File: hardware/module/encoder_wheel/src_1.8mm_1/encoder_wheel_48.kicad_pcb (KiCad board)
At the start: 2 copper layers, 74 x 74 mm, 2 parts

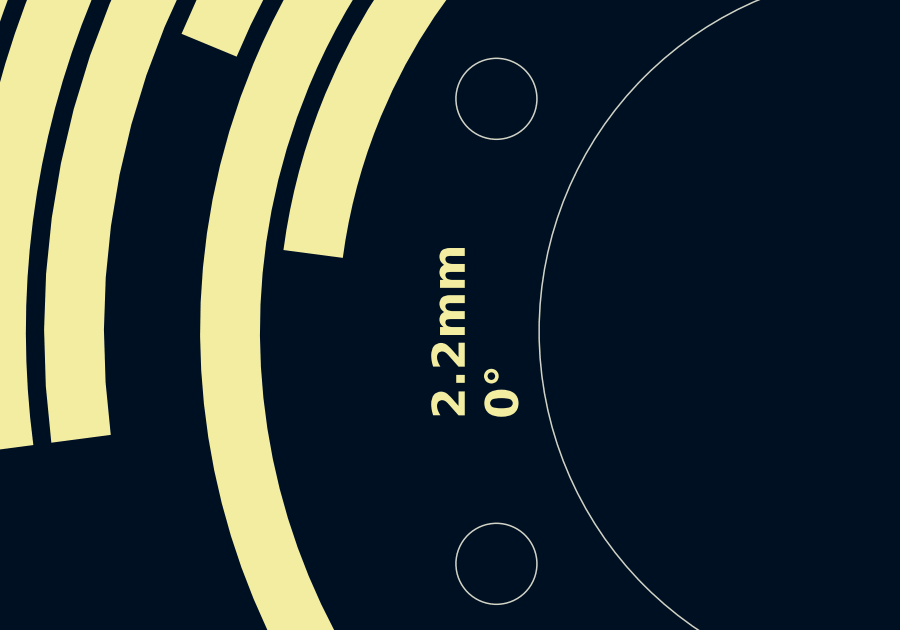
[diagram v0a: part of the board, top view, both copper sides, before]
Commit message: add encoder wheel variants
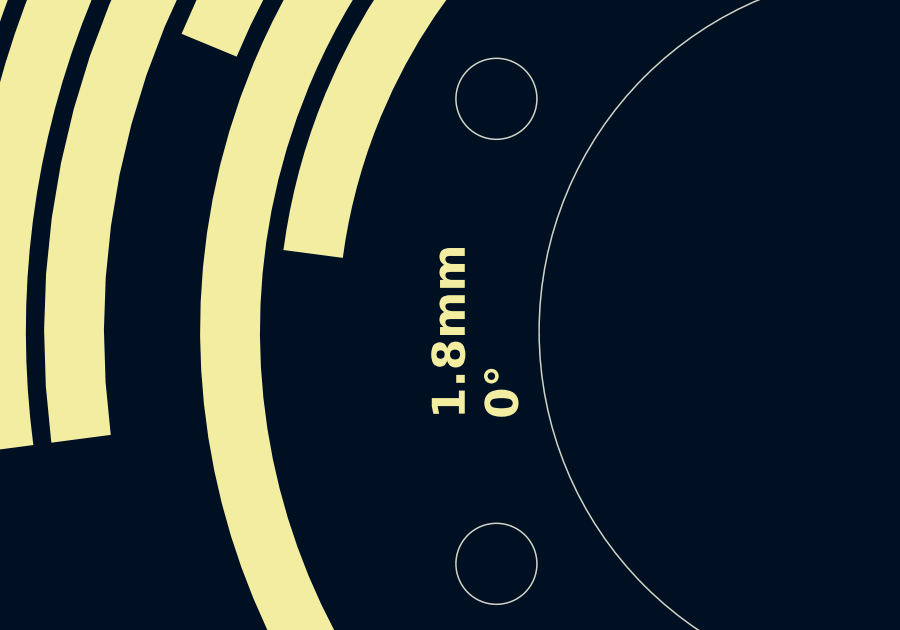
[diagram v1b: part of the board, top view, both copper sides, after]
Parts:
- REF** (x2): value OpenFlapEncoderPattern48_2.2mm -> OpenFlapEncoderPattern48_1.8mm; footprint EncoderPattern:OpenFlapEncoderPattern48_2.2mm -> EncoderPattern:OpenFlapEncoderPattern48_1.8mm
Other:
- board text added: "1.8mm 0°"
- board text added: "1.8mm 3.75°"
- board text removed: "2.2mm 0°"
- board text removed: "2.2mm 3.75°"
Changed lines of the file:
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@@
 	)
 	(net 0 "")
-	(footprint "EncoderPattern:OpenFlapEncoderPattern48_2.2mm"
+	(footprint "EncoderPattern:OpenFlapEncoderPattern48_1.8mm"
 		(layer "F.Cu")
 		(at 101 100)
@@
 			)
 		)
-		(property "Value" "OpenFlapEncoderPattern48_2.2mm"
+		(property "Value" "OpenFlapEncoderPattern48_1.8mm"
 			(at 0 1 0)
 			(unlocked yes)
@@
 			)
 		)
-		(property "Footprint" "EncoderPattern:OpenFlapEncoderPattern48_2.2mm"
+		(property "Footprint" "EncoderPattern:OpenFlapEncoderPattern48_1.8mm"
 			(at 0 0 0)
 			(unlocked yes)
@@
 		)
 	)
-	(footprint "EncoderPattern:OpenFlapEncoderPattern48_2.2mm"
+	(footprint "EncoderPattern:OpenFlapEncoderPattern48_1.8mm"
 		(layer "B.Cu")
 		(at 101 100 -176.25)
@@
 			)
 		)
-		(property "Value" "OpenFlapEncoderPattern48_2.2mm"
+		(property "Value" "OpenFlapEncoderPattern48_1.8mm"
 			(at 0 -1 3.75)
 			(unlocked yes)
@@
 			)
 		)
-		(property "Footprint" "EncoderPattern:OpenFlapEncoderPattern48_2.2mm"
+		(property "Footprint" "EncoderPattern:OpenFlapEncoderPattern48_1.8mm"
 			(at 0 0 3.75)
 			(unlocked yes)
@@
 		(layer "Edge.Cuts")
 	)
-	(gr_text "2.2mm \n3.75°"
+	(gr_text "1.8mm \n3.75°"
 		(at 88.427 97.333 90)
 		(layer "B.SilkS")
@@
 		)
 	)
-	(gr_text "2.2mm \n0°"
+	(gr_text "1.8mm \n0°"
 		(at 88.427 102.921 90)
 		(layer "F.SilkS")

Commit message: encoder changes
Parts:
- renumbered REF** to ENC1, REF** to ENC2

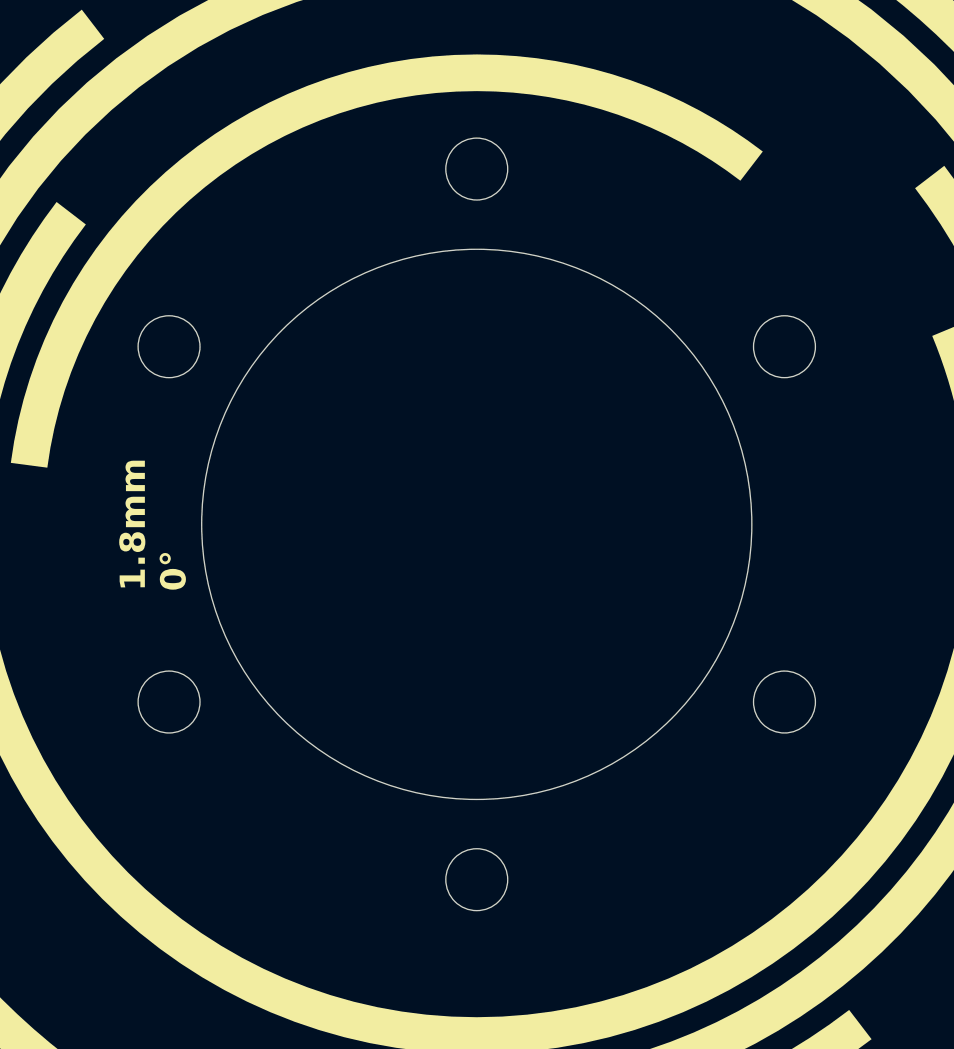
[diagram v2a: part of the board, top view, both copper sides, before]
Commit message: changed hole patern encoder wheel
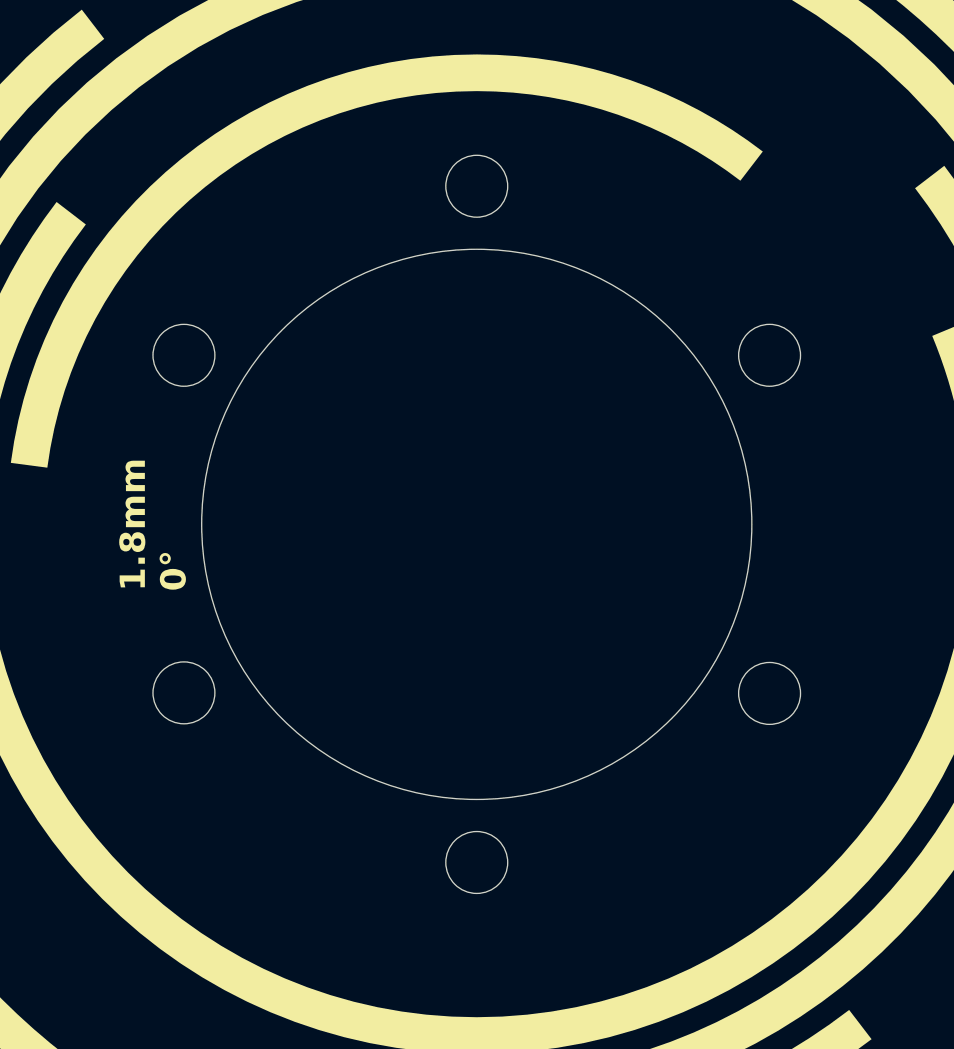
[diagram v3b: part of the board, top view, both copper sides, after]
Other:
- outline, holes or cut-outs redrawn
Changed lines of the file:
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@@
 				(xy -11.266715 -29.849949) (xy -10.281481 -30.203466) (xy -9.281621 -30.525345) (xy -8.267751 -30.81502)
 				(xy -8.682197 -32.362208) (xy -9.747476 -32.058296) (xy -10.797996 -31.720567) (xy -11.833111 -31.349614)
-				(xy -12.852178 -30.946031) (xy -13.854554 -30.510402) (xy -14.839593 -30.043327) (xy -15.806652 -29.545395)
+				(xy -12.852178 -30.946032) (xy -13.854554 -30.510402) (xy -14.839593 -30.043327) (xy -15.806652 -29.545395)
 				(xy -16.755088 -29.017199) (xy -15.952037 -27.627619)
 			)
@@
 				(xy 8.661965 -32.367899) (xy 7.619346 -32.628167) (xy 6.564163 -32.855757) (xy 5.496965 -33.050046)
 				(xy 4.4183 -33.21041) (xy 3.328719 -33.336223) (xy 2.228768 -33.426863) (xy 1.118999 -33.481705)
-				(xy -0.000041 -33.500124) (xy -0.001075 -33.500124) (xy -0.000556 -31.900225) (xy -0.000041 -31.900222)
+				(xy -0.000041 -33.500124) (xy -0.001075 -33.500124) (xy -0.000556 -31.900225) (xy -0.000041 -31.90022)
 				(xy 1.065218 -31.882664) (xy 2.121714 -31.830376) (xy 3.168918 -31.743958) (xy 4.2063 -31.624002)
 				(xy 5.23333 -31.471104) (xy 6.249476 -31.285859) (xy 7.254211 -31.06886) (xy 8.247002 -30.820704)
@@
 				(xy -23.637434 -21.416908) (xy -23.284883 -21.799537) (xy -22.926198 -22.176364) (xy -22.561452 -22.547308)
 				(xy -23.697817 -23.682639) (xy -24.457612 -22.897228) (xy -25.191642 -22.087376) (xy -25.899258 -21.253758)
-				(xy -26.579808 -20.39705) (xy -27.232652 -19.517927) (xy -27.857134 -18.617065) (xy -28.452607 -17.695141)
+				(xy -26.579806 -20.39705) (xy -27.232652 -19.517927) (xy -27.857134 -18.617065) (xy -28.452607 -17.695141)
 				(xy -29.018422 -16.752829) (xy -27.62781 -15.950812)
 			)
@@
 			(pts
 				(xy 18.806561 -24.521345) (xy 18.008705 -25.113995) (xy 17.19143 -25.681322) (xy 16.355315 -26.222746)
-				(xy 15.500938 -26.737683) (xy 14.628876 -27.225549) (xy 13.739707 -27.685761) (xy 12.834011 -28.117743)
+				(xy 15.500938 -26.737683) (xy 14.628876 -27.225549) (xy 13.739707 -27.685759) (xy 12.834011 -28.117743)
 				(xy 11.912364 -28.520903) (xy 10.975345 -28.894663) (xy 10.023531 -29.23844) (xy 9.057502 -29.551649)
 				(xy 8.077834 -29.83371) (xy 7.085106 -30.084038) (xy 6.079895 -30.302052) (xy 5.062781 -30.487168)
@@
 				(xy -17.828925 23.247311) (xy -18.806127 24.521135) (xy -18.008283 25.11377) (xy -17.191027 25.681088)
 				(xy -16.354937 26.222504) (xy -15.500589 26.737436) (xy -14.628561 27.225301) (xy -13.73943 27.685516)
-				(xy -12.833772 28.117497) (xy -11.912166 28.520661) (xy -10.975189 28.894428) (xy -10.023417 29.238206)
-				(xy -9.057427 29.551421) (xy -8.077795 29.833486) (xy -7.085104 30.083819) (xy -6.079929 30.301836)
+				(xy -12.833772 28.117497) (xy -11.912166 28.520661) (xy -10.975189 28.894429) (xy -10.023417 29.238206)
+				(xy -9.057427 29.551421) (xy -8.077795 29.833486) (xy -7.085104 30.083819) (xy -6.07993 30.301836)
 				(xy -5.062838 30.486955) (xy -4.034419 30.638591)
 			)
@@
 				(xy -17.090735 -23.796679) (xy -16.304792 -24.343111) (xy -15.500463 -24.864257) (xy -14.678322 -25.359541)
 				(xy -13.838943 -25.828387) (xy -12.982901 -26.270221) (xy -12.110771 -26.684465) (xy -11.223127 -27.070544)
-				(xy -11.837043 -28.552111) (xy -12.773694 -28.145174) (xy -13.693928 -27.70851) (xy -14.597134 -27.242726)
+				(xy -11.837043 -28.552111) (xy -12.773694 -28.145174) (xy -13.69393 -27.70851) (xy -14.597134 -27.242726)
 				(xy -15.482717 -26.748428) (xy -16.350072 -26.226223) (xy -17.198594 -25.676718) (xy -18.02768 -25.10052)
-				(xy -18.836728 -24.498237) (xy -19.625135 -23.870473) (xy -20.392296 -23.217837) (xy -21.137612 -22.540936)
+				(xy -18.836728 -24.498237) (xy -19.625135 -23.870473) (xy -20.392296 -23.217837) (xy -21.137613 -22.540936)
 				(xy -21.860471 -21.840376) (xy -22.560278 -21.116764) (xy -23.236427 -20.370707) (xy -23.888314 -19.602811)
 				(xy -24.515338 -18.813685) (xy -23.24203 -17.835966)
@@
 				(xy 22.135658 14.92714) (xy 21.120306 16.329401) (xy 20.018367 17.661261) (xy 18.833957 18.918605)
 				(xy 17.571194 20.097317) (xy 16.234196 21.193282) (xy 14.827081 22.202386) (xy 13.353966 23.120514)
-				(xy 11.818969 23.94355) (xy 10.226209 24.66738) (xy 10.84116 26.149976)
+				(xy 11.818969 23.94355) (xy 10.226209 24.66738) (xy 10.841161 26.149976)
 			)
 			(stroke
@@
 				(xy -28.296811 -0.467562) (xy -28.300636 0.000154) (xy -28.250268 1.703391) (xy -28.101061 3.379906)
 				(xy -27.855866 5.026858) (xy -27.517533 6.641405) (xy -27.088911 8.220705) (xy -26.572849 9.761917)
-				(xy -25.972198 11.2622) (xy -25.289807 12.718712) (xy -24.528525 14.128612) (xy -23.691206 15.489057)
+				(xy -25.972198 11.2622) (xy -25.289807 12.718712) (xy -24.528525 14.128612) (xy -23.691208 15.489057)
 				(xy -22.78069 16.797208) (xy -21.799835 18.050221) (xy -20.751489 19.245257) (xy -19.6385 20.379472)
 				(xy -18.463719 21.450027) (xy -17.229995 22.454078)
@@
 				(xy -29.237832 -1.924824) (xy -29.202875 -2.401023) (xy -29.160371 -2.875098) (xy -29.110401 -3.346999)
 				(xy -29.053045 -3.816668) (xy -30.639512 -4.025443) (xy -30.699902 -3.530123) (xy -30.752548 -3.03244)
-				(xy -30.797354 -2.532453) (xy -30.834229 -2.030208) (xy -30.863069 -1.525771) (xy -30.883788 -1.019194)
+				(xy -30.797354 -2.532454) (xy -30.83423 -2.030208) (xy -30.863069 -1.525771) (xy -30.883788 -1.019194)
 				(xy -30.896289 -0.510533) (xy -30.900478 0.000154) (xy -30.890729 0.78352) (xy -30.861641 1.56206)
 				(xy -30.813448 2.335546) (xy -30.746385 3.103753) (xy -30.660688 3.866454) (xy -30.556591 4.62342)
@@
 				(xy -10.83142 -26.153803) (xy -10.216987 -24.67121) (xy -9.623267 -24.909187) (xy -9.022652 -25.133286)
 				(xy -8.415338 -25.343305) (xy -7.801522 -25.539039) (xy -7.1814 -25.720284) (xy -6.555168 -25.886838)
-				(xy -5.923023 -26.038495) (xy -5.285163 -26.175054) (xy -4.641777 -26.296309) (xy -3.993074 -26.402058)
+				(xy -5.923023 -26.038495) (xy -5.285163 -26.175054) (xy -4.641775 -26.296309) (xy -3.993074 -26.402058)
 				(xy -3.339241 -26.492097) (xy -2.680477 -26.566221) (xy -2.016979 -26.624228) (xy -1.348942 -26.665914)
 				(xy -0.676564 -26.691075) (xy -0.000041 -26.699507) (xy 1.140178 -26.675552) (xy 2.268208 -26.604328)
@@
 				(xy 11.013382 -20.312902) (xy 10.017318 -20.822849) (xy 8.993996 -21.285266) (xy 7.944866 -21.698708)
 				(xy 6.871376 -22.061717) (xy 5.774973 -22.372854) (xy 4.657106 -22.630667) (xy 3.519223 -22.83371)
-				(xy 2.362772 -22.980533) (xy 1.189201 -23.069689) (xy -0.000041 -23.09973) (xy -1.189285 -23.069689)
+				(xy 2.362772 -22.980533) (xy 1.189201 -23.069689) (xy -0.000041 -23.09973) (xy -1.189286 -23.069689)
 				(xy -2.362848 -22.980533) (xy -3.519292 -22.83371) (xy -4.657166 -22.630667) (xy -5.775021 -22.372854)
 				(xy -6.871409 -22.061717) (xy -7.944884 -21.698705) (xy -8.993996 -21.285266) (xy -10.017299 -20.822849)
@@
 	)
 	(gr_circle
-		(center 87.576606 107.75)
-		(end 88.926606 107.75)
+		(center 88.226125 107.35)
+		(end 89.576125 107.35)
 		(stroke
 			(width 0.05)
@@
 	)
 	(gr_circle
-		(center 101 84.5)
-		(end 102.35 84.5)
-		(stroke
-			(width 0.05)
-			(type default)
-		)
-		(fill none)
-		(layer "Edge.Cuts")
-	)
-	(gr_circle
-		(center 114.423394 92.25)
-		(end 115.773394 92.25)
-		(stroke
-			(width 0.05)
-			(type default)
-		)
-		(fill none)
-		(layer "Edge.Cuts")
-	)
-	(gr_circle
-		(center 87.576606 92.25)
-		(end 88.926606 92.25)
+		(center 101 85.25)
+		(end 102.35 85.25)
+		(stroke
+			(width 0.05)
+			(type default)
+		)
+		(fill none)
+		(layer "Edge.Cuts")
+	)
+	(gr_circle
+		(center 113.773875 92.625)
+		(end 115.123875 92.625)
+		(stroke
+			(width 0.05)
+			(type default)
+		)
+		(fill none)
+		(layer "Edge.Cuts")
+	)
+	(gr_circle
+		(center 88.226125 92.625)
+		(end 89.576125 92.625)
 		(stroke
 			(width 0.05)
@@
 	)
 	(gr_circle
-		(center 114.423394 107.75)
-		(end 115.773394 107.75)
-		(stroke
-			(width 0.05)
-			(type default)
-		)
-		(fill none)
-		(layer "Edge.Cuts")
-	)
-	(gr_circle
-		(center 101 115.5)
-		(end 102.35 115.5)
-		(stroke
-			(width 0.05)
+		(center 113.773875 107.375)
+		(end 115.123875 107.375)
+		(stroke
+			(width 0.05)
+			(type default)
+		)
+		(fill none)
+		(layer "Edge.Cuts")
+	)
+	(gr_circle
+		(center 101 114.75)
+		(end 102.35 114.75)
+		(stroke
+			(width 0.05)
